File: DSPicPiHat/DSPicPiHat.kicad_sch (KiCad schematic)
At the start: 40 parts

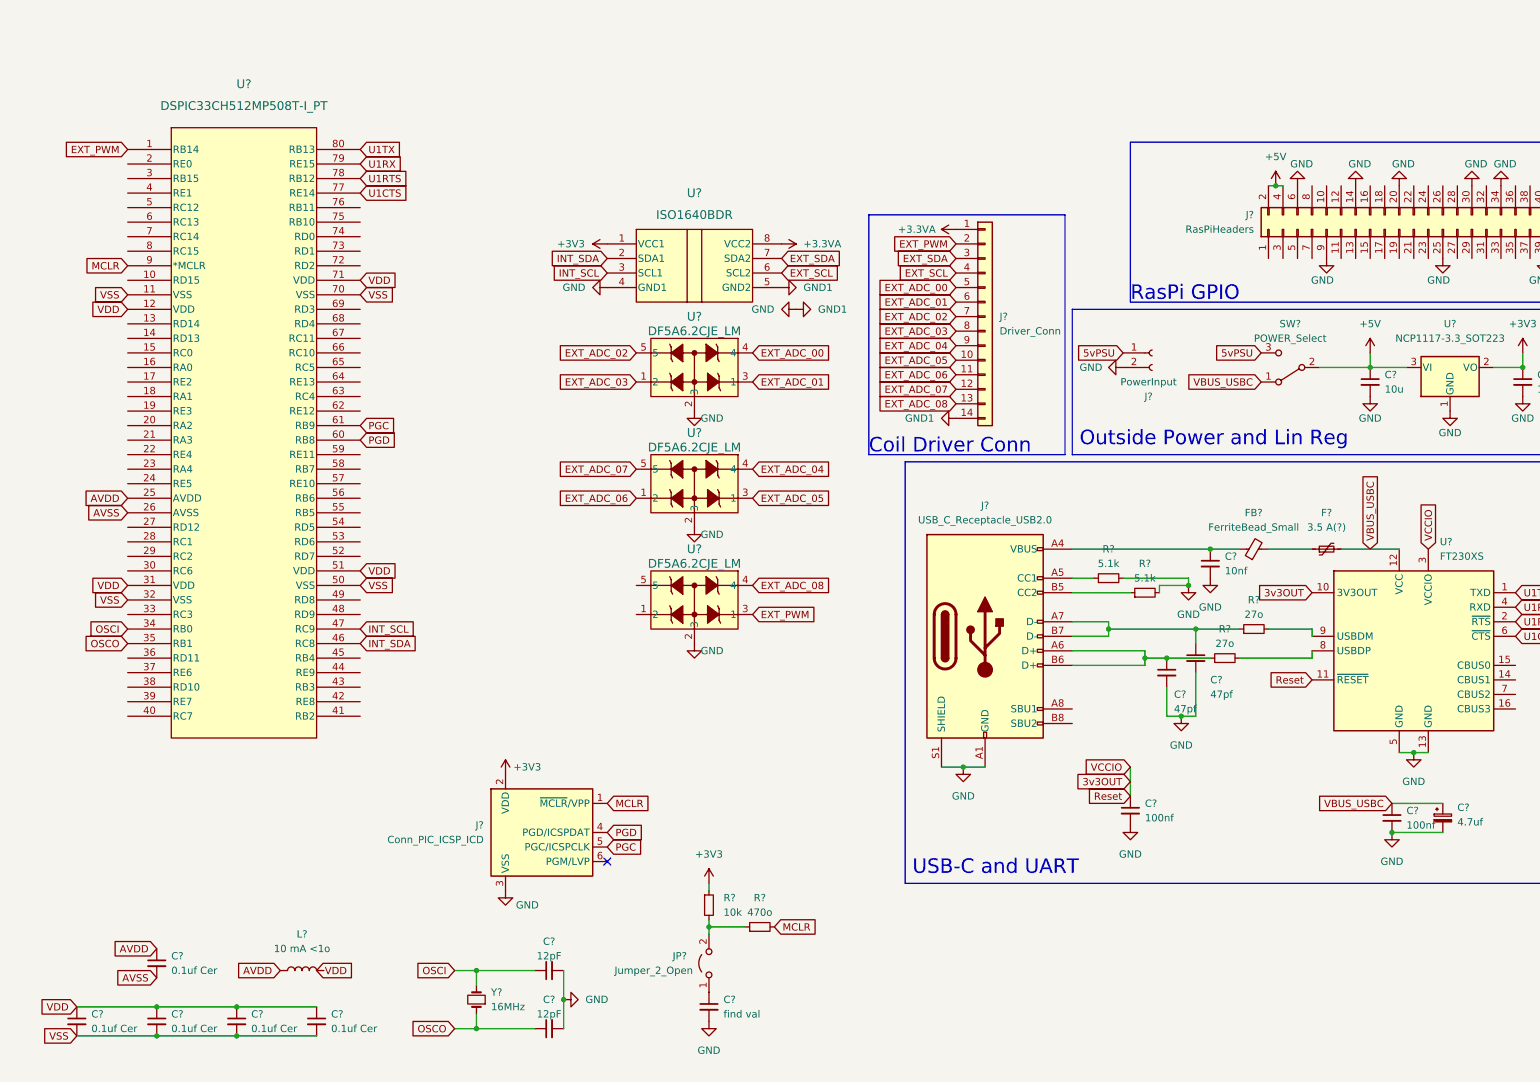
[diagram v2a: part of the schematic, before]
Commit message: Wire ADC to dsPIC, moved things around.
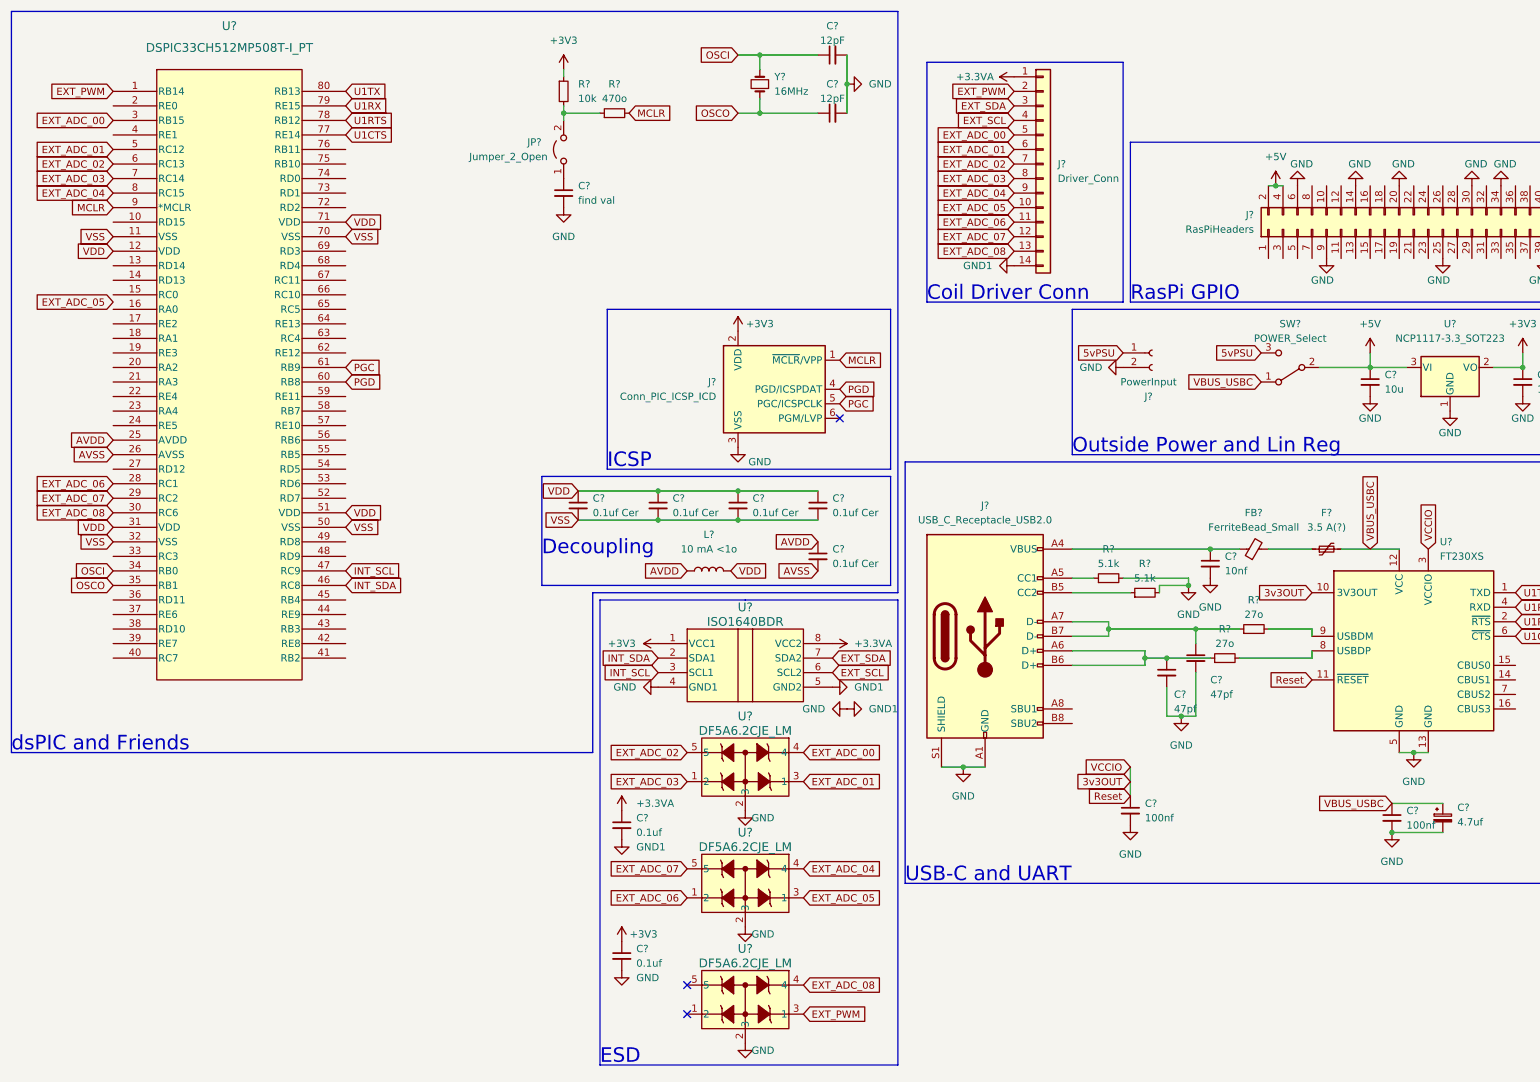
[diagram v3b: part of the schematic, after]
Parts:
- added C? (x2): 0.1uf, symbol Device:C_Small
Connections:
- net +3.3VA: now also C?.1
- net +3V3: now also C?.1
- net EXT_ADC_00: now also U?.3 (RB15)
- net EXT_ADC_01: now also U?.5 (RC12)
- net EXT_ADC_02: now also U?.6 (RC13)
- net EXT_ADC_03: now also U?.7 (RC14)
- net EXT_ADC_04: now also U?.8 (RC15)
- net EXT_ADC_06: now also U?.28 (RC1)
- net EXT_ADC_07: now also U?.29 (RC2)
- net EXT_ADC_08: now also U?.30 (RC6)
- net GND: now also C?.2, C?.2
- net VDD: now also L?.2
- no-connect marks 1 -> 3
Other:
- note added: "Decoupling"
- note added: "ESD"
- note added: "ICSP"
- note added: "dsPIC and Friends"
- moved on the sheet: C?, J?, JP?, L?, R?, U?, Y?

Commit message: each axis needs own conn
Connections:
- removed net EXT_ADC_00: J?.5 (Pin_5), U?.3 (RB15), U?.4
- removed net EXT_ADC_01: J?.6 (Pin_6), U?.3 (1), U?.5 (RC12)
- removed net EXT_ADC_02: J?.7 (Pin_7), U?.5, U?.6 (RC13)
- removed net EXT_ADC_03: J?.8 (Pin_8), U?.1 (2), U?.7 (RC14)
- removed net EXT_ADC_04: J?.9 (Pin_9), U?.4, U?.8 (RC15)
- net EXT_ADC_05: no longer names the net of U?.3 (1)
- net EXT_ADC_05: no longer J?.10 (Pin_10)
- removed net EXT_ADC_06: J?.11 (Pin_11), U?.1 (2), U?.28 (RC1)
- removed net EXT_ADC_07: J?.12 (Pin_12), U?.29 (RC2), U?.5
- removed net EXT_ADC_08: J?.13 (Pin_13), U?.30 (RC6), U?.4
- removed net EXT_PWM: J?.2 (Pin_2), U?.1 (RB14), U?.3 (1)
- net EXT_SCL renamed EXT_X_SCL
- net EXT_SDA renamed EXT_X_SDA
- net INT_SCL: no longer names the net of U?.47 (RC9)
- net INT_SCL: no longer U?.3 (SCL1)
- net INT_SDA: no longer names the net of U?.46 (RC8)
- net INT_SDA: no longer U?.2 (SDA1)
- new net EXT_ADC_X_00: J?.5 (Pin_5)
- new net EXT_ADC_X_01: J?.6 (Pin_6)
- new net EXT_ADC_X_02: J?.7 (Pin_7)
- new net EXT_ADC_X_03: J?.8 (Pin_8)
- new net EXT_ADC_X_04: J?.9 (Pin_9)
- new net EXT_ADC_X_05: J?.10 (Pin_10)
- new net EXT_ADC_X_06: J?.11 (Pin_11)
- new net EXT_ADC_X_07: J?.12 (Pin_12)
- new net EXT_ADC_X_08: J?.13 (Pin_13)
- new net EXT_X_PWM: J?.2 (Pin_2)
- new net INT_X_SCL: U?.3 (SCL1)
- new net INT_X_SDA: U?.2 (SDA1)
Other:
- note added: "Coil Driver Conn X"
- note removed: "Coil Driver Conn"
- moved on the sheet: C?, F?, FB?, J?, R?, SW?, U?

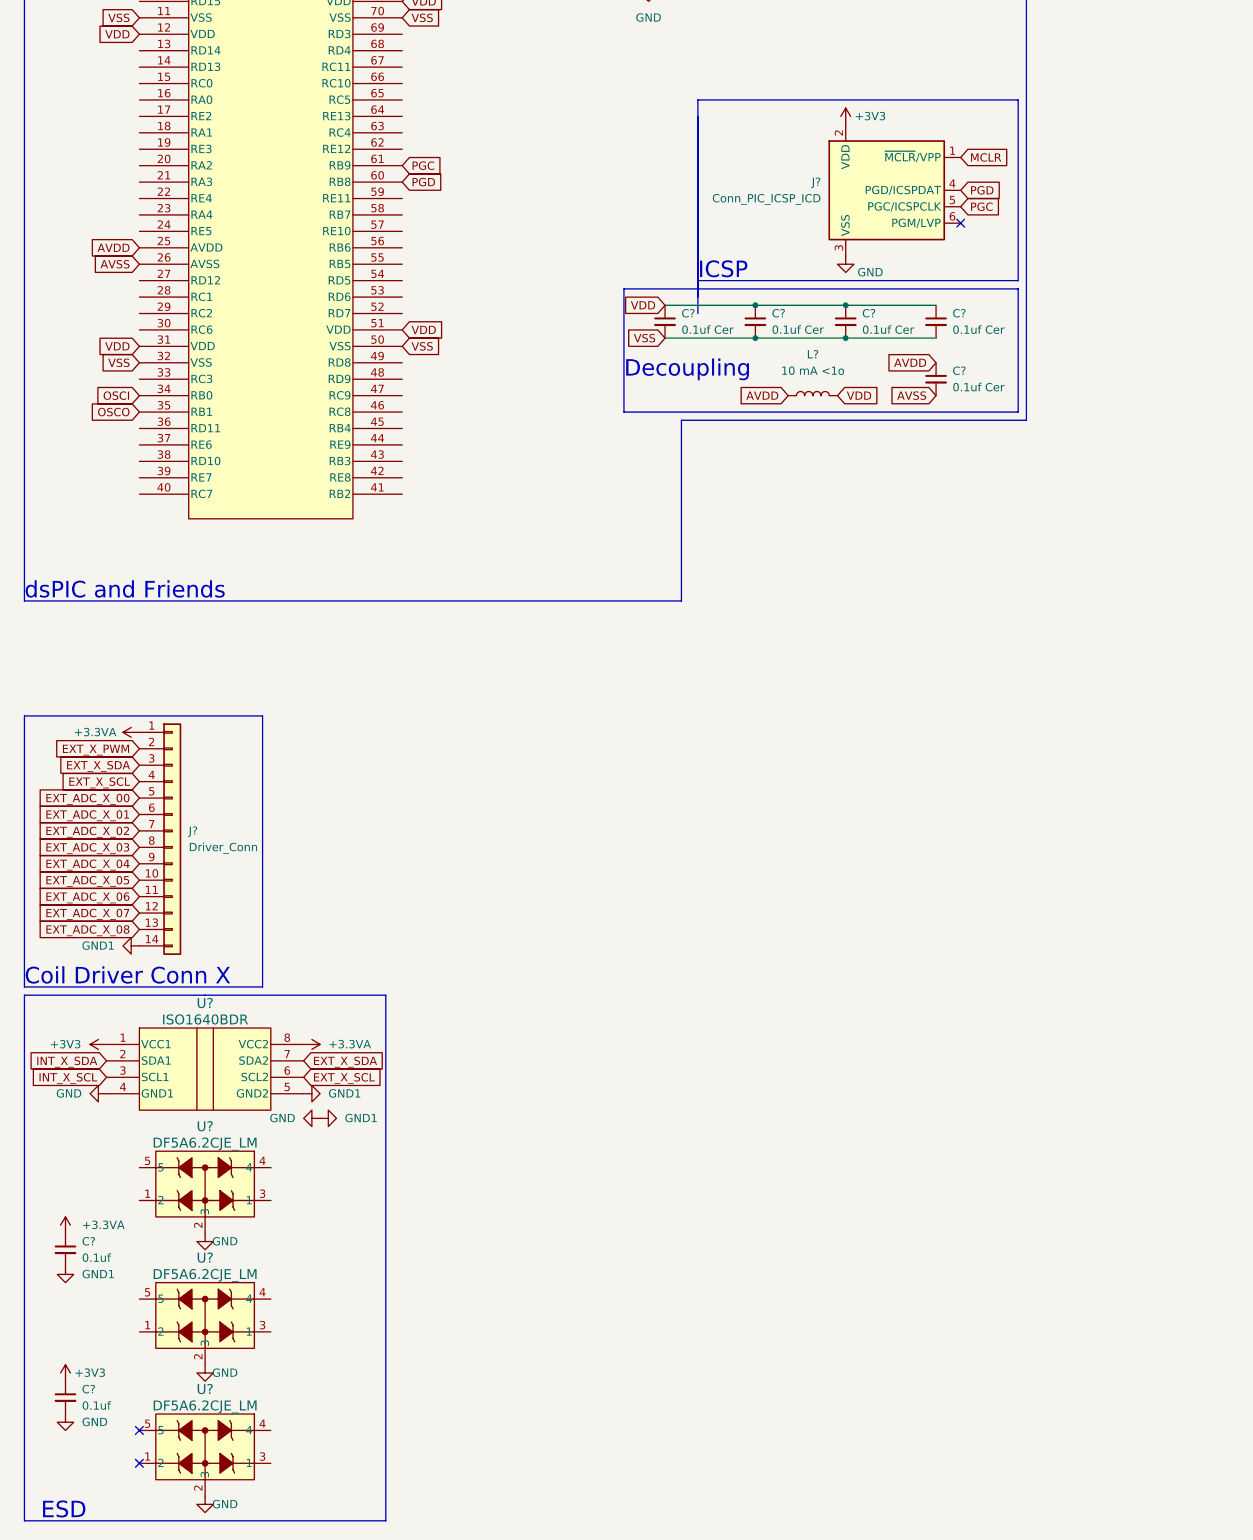
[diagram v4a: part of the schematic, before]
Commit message: more coil driver headers and protection
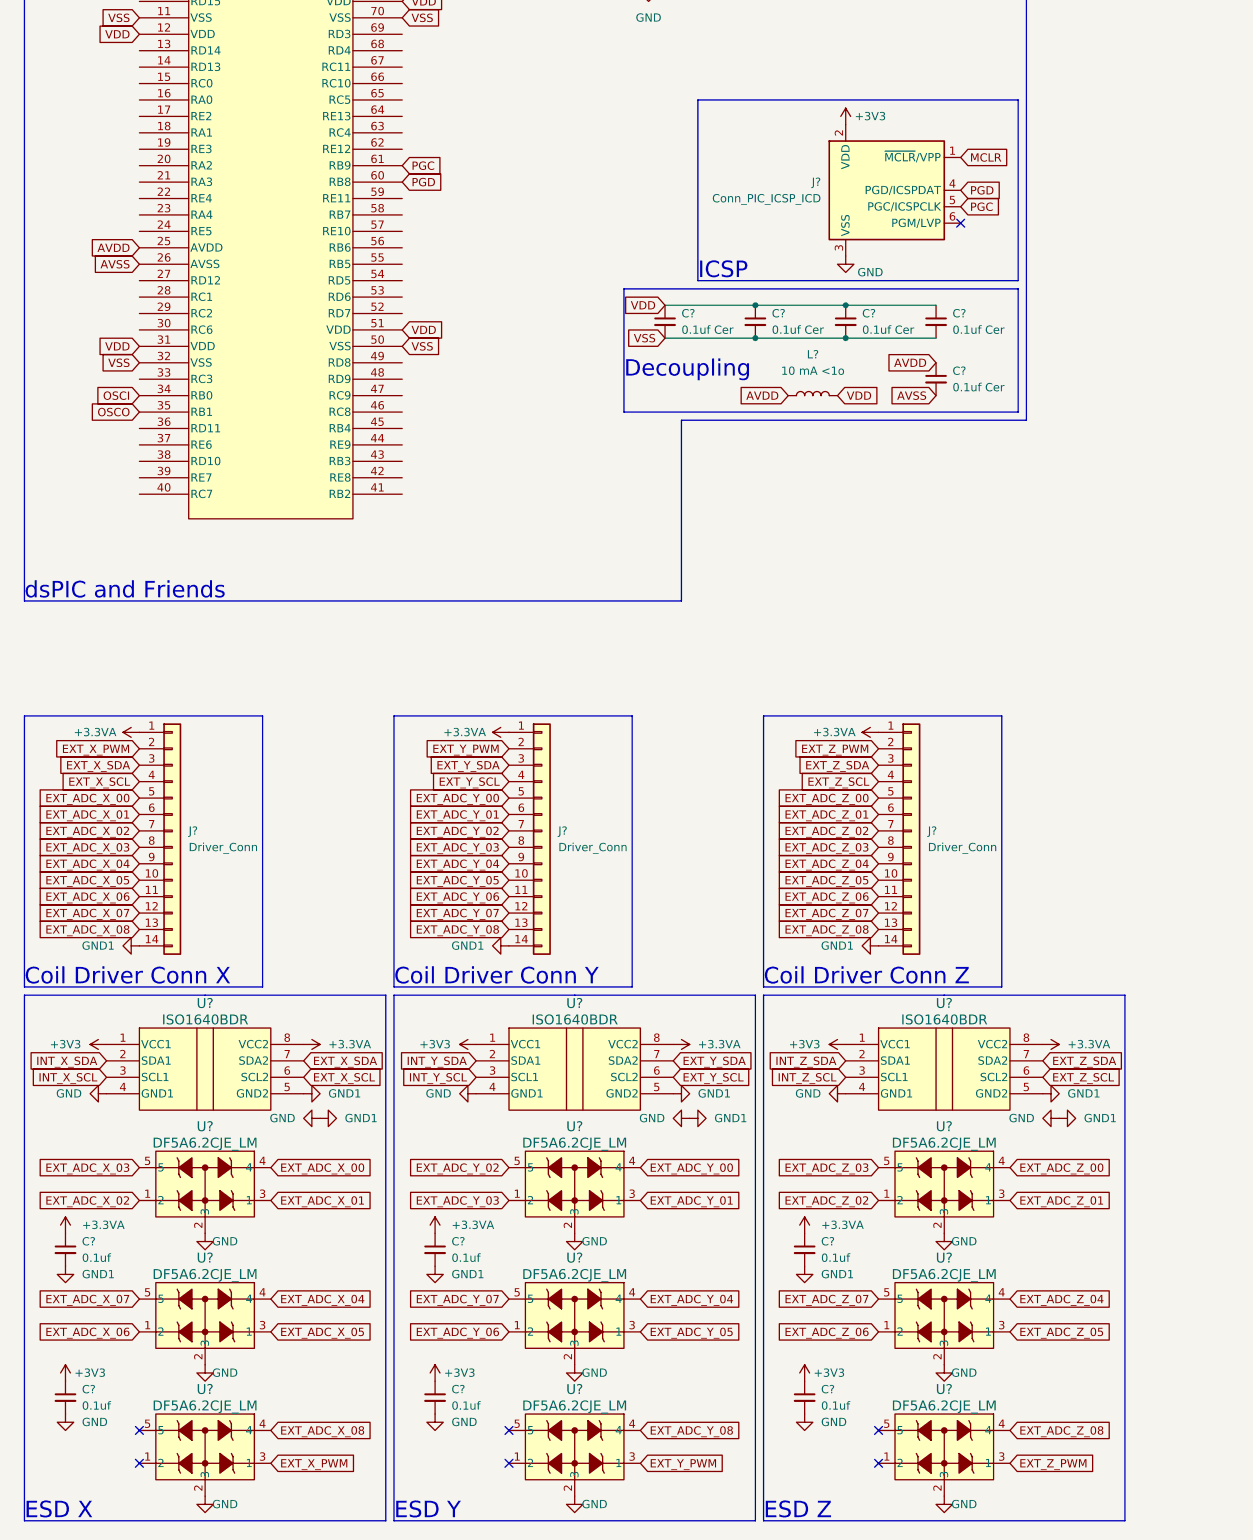
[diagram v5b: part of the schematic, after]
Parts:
- added C? (x4): 0.1uf, symbol Device:C_Small
- added J? (x2): Driver_Conn, symbol Connector_Generic:Conn_01x14
- added U? (x2): ISO1640BDR, D0008B-IPC_A, symbol PiHatLib:ISO1640BDR
- added U? (x6): DF5A6.2CJE_LM, SOT-553 ESV_TOS, symbol PiHatLib:DF5A6.2CJE_LM
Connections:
- net +3.3VA: now also C?.1, C?.1, J?.1 (Pin_1), J?.1 (Pin_1), U?.8 (VCC2), U?.8 (VCC2)
- net +3V3: now also C?.1, C?.1, U?.1 (VCC1), U?.1 (VCC1)
- net EXT_ADC_X_00: now also U?.4
- net EXT_ADC_X_01: now also U?.3 (1)
- net EXT_ADC_X_02: now also U?.1 (2)
- net EXT_ADC_X_03: now also U?.5
- net EXT_ADC_X_04: now also U?.4
- net EXT_ADC_X_05: now also U?.3 (1)
- net EXT_ADC_X_06: now also U?.1 (2)
- net EXT_ADC_X_07: now also U?.5
- net EXT_ADC_X_08: now also U?.4
- net EXT_X_PWM: now also U?.3 (1)
- net GND: now also C?.2, C?.2, C?.2, C?.2, J?.14 (Pin_14), J?.14 (Pin_14), U?.2 (3), U?.2 (3), U?.2 (3), U?.2 (3), U?.2 (3), U?.2 (3), U?.4 (GND1), U?.4 (GND1), U?.5 (GND2), U?.5 (GND2)
- new net EXT_ADC_Y_00: J?.5 (Pin_5), U?.4
- new net EXT_ADC_Y_01: J?.6 (Pin_6), U?.3 (1)
- new net EXT_ADC_Y_02: J?.7 (Pin_7), U?.5
- new net EXT_ADC_Y_03: J?.8 (Pin_8), U?.1 (2)
- new net EXT_ADC_Y_04: J?.9 (Pin_9), U?.4
- new net EXT_ADC_Y_05: J?.10 (Pin_10), U?.3 (1)
- new net EXT_ADC_Y_06: J?.11 (Pin_11), U?.1 (2)
- new net EXT_ADC_Y_07: J?.12 (Pin_12), U?.5
- new net EXT_ADC_Y_08: J?.13 (Pin_13), U?.4
- new net EXT_ADC_Z_00: J?.5 (Pin_5), U?.4
- new net EXT_ADC_Z_01: J?.6 (Pin_6), U?.3 (1)
- new net EXT_ADC_Z_02: J?.7 (Pin_7), U?.1 (2)
- new net EXT_ADC_Z_03: J?.8 (Pin_8), U?.5
- new net EXT_ADC_Z_04: J?.9 (Pin_9), U?.4
- new net EXT_ADC_Z_05: J?.10 (Pin_10), U?.3 (1)
- new net EXT_ADC_Z_06: J?.11 (Pin_11), U?.1 (2)
- new net EXT_ADC_Z_07: J?.12 (Pin_12), U?.5
- new net EXT_ADC_Z_08: J?.13 (Pin_13), U?.4
- new net EXT_Y_PWM: J?.2 (Pin_2), U?.3 (1)
- new net EXT_Y_SCL: J?.4 (Pin_4), U?.6 (SCL2)
- new net EXT_Y_SDA: J?.3 (Pin_3), U?.7 (SDA2)
- new net EXT_Z_PWM: J?.2 (Pin_2), U?.3 (1)
- new net EXT_Z_SCL: J?.4 (Pin_4), U?.6 (SCL2)
- new net EXT_Z_SDA: J?.3 (Pin_3), U?.7 (SDA2)
- new net INT_Y_SCL: U?.3 (SCL1)
- new net INT_Y_SDA: U?.2 (SDA1)
- new net INT_Z_SCL: U?.3 (SCL1)
- new net INT_Z_SDA: U?.2 (SDA1)
- no-connect marks 3 -> 7
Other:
- note added: "Coil Driver Conn Y"
- note added: "Coil Driver Conn Z"
- note added: "ESD X"
- note added: "ESD Y"
- note added: "ESD Z"
- note removed: "ESD"
